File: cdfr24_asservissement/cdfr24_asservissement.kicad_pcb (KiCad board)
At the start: 2 copper layers, 102 x 82.8 mm, 106 parts, among them J1 Connecteur batterie, J10 Conn_01x05, J11 Conn_01x03, J12 Conn_01x05, J13 Conn_01x03, J14 Conn_ST_STDC14, J15 Free Connecteur, J2 Conn_01x03, J3 Connecteur Programmation, J4 Connecteur Odométrie, J5 Free Connecteur, J6 Connecteur Odométrie, J7 Conn_01x03, J8 Conn_01x02, J9 Conn_01x02, Q1 Q_NMOS_GDS, U1 LM317_SOT-223, U2 LMR16020PDDA, U3 STM32F401RCTx, U4 LSM6DSL, Y1 Crystal_GND24

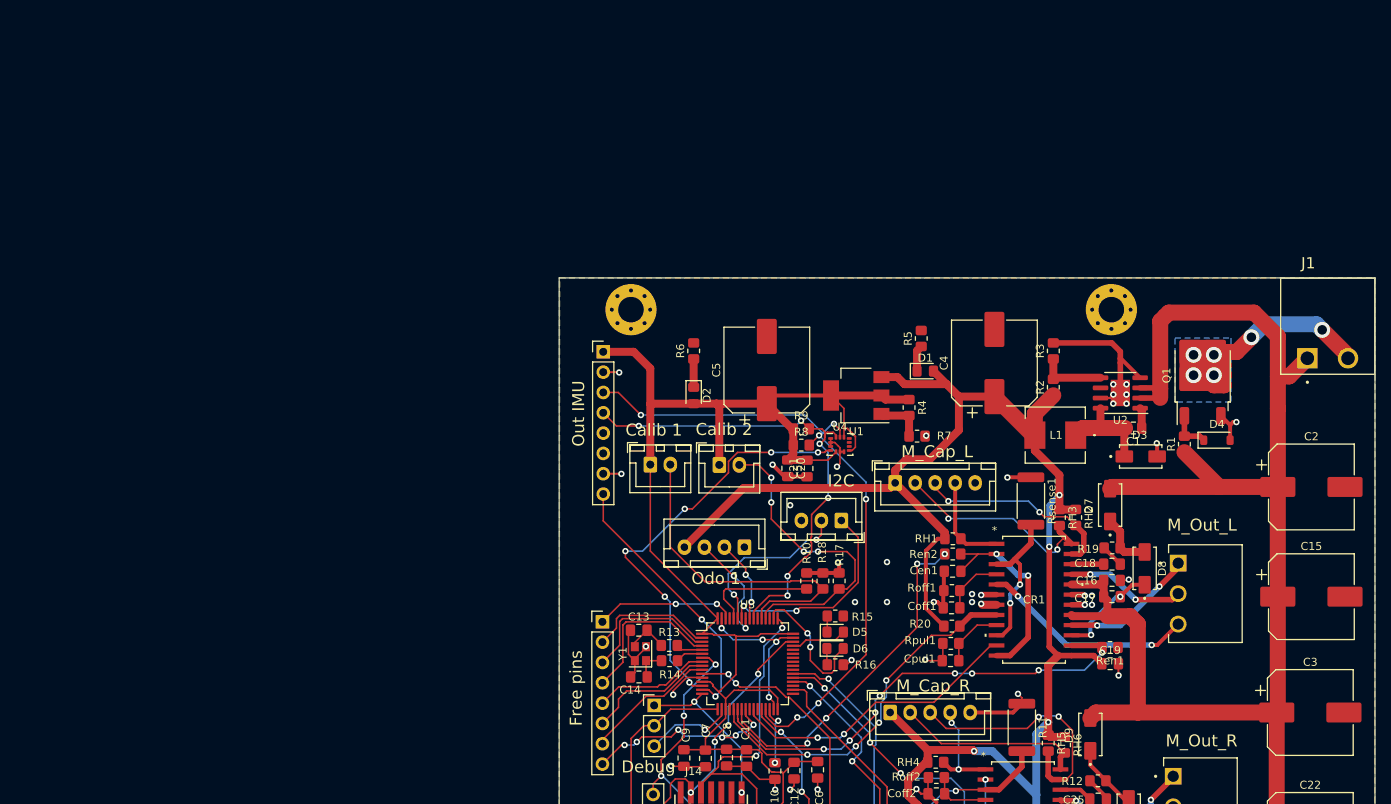
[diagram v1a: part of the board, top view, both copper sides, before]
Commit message: Change 5v to 3.3v regulator to ST product
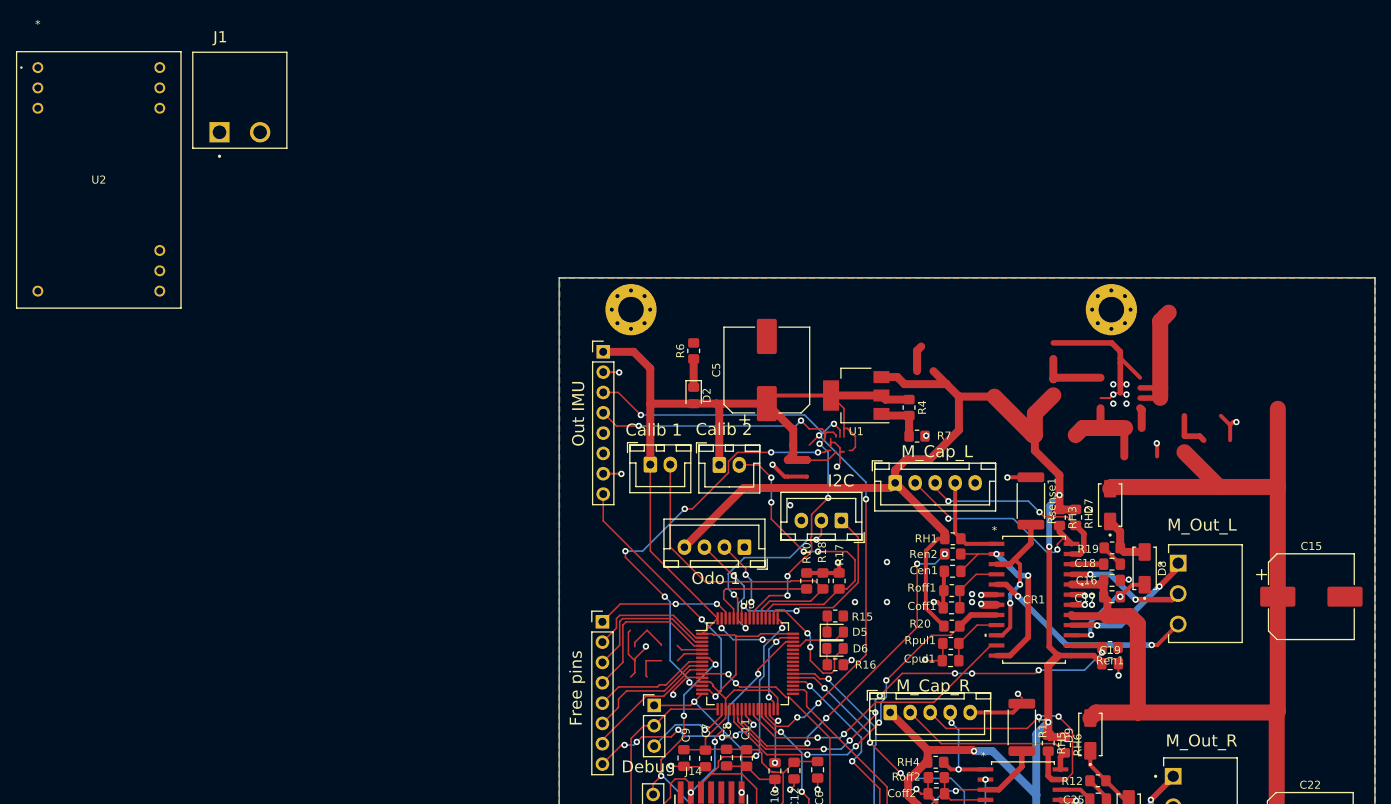
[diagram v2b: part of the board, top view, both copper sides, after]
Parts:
- removed C1, C20, C21: 100nF, Capacitor_SMD:C_0805_2012Metric_Pad1.18x1.45mm_HandSolder
- removed C13, C14: 10pF, Capacitor_SMD:C_0805_2012Metric_Pad1.18x1.45mm_HandSolder
- removed C2, C3: 470uF, Capacitor_SMD:CP_Elec_10x10.5
- removed C4: 220uF, Capacitor_SMD:CP_Elec_10x10.5
- removed D1: LED, LED_SMD:LED_0805_2012Metric_Pad1.15x1.40mm_HandSolder
- removed D3: DIODE, B170B:DIOM505270X240
- removed D4: D_Zener, Diode_SMD:D_SOD-123
- removed L1: 10uH, IHLP2525CZER100M01:IND_IHLP_2525_CZ-M
- removed Q1: Q_NMOS_GDS, Package_TO_SOT_SMD:TO-252-2
- removed R1, R2, R8, R9: 56k, Resistor_SMD:R_0805_2012Metric_Pad1.20x1.40mm_HandSolder
- removed R13, R14, R3: 10k, Resistor_SMD:R_0805_2012Metric_Pad1.20x1.40mm_HandSolder
- removed R5: 220, Resistor_SMD:R_0805_2012Metric_Pad1.20x1.40mm_HandSolder
- removed U4: LSM6DSL, Package_LGA:LGA-14_3x2.5mm_P0.5mm_LayoutBorder3x4y
- removed Y1: Crystal_GND24, Crystal:Crystal_SMD_2520-4Pin_2.5x2.0mm
- U2: value LMR16020PDDA -> TVN 5-2411WI; footprint Package_SO:SOIC-8-1EP_3.9x4.9mm_P1.27mm_EP2.41x3.3mm -> TVN_5WI_SINGLE_TRP:TVN_5WI_SINGLE_TRP
- moved U2 141.3 mm to (2.86, 2.19), turned to 0 degrees
- moved J1 138.9 mm to (25.6, 10.3)
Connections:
- J1 pad 2: /InputVoltage -> GND
- J15 pad 8: /IMU_INT2 -> /IMU_INT1
- U2 pad 1: Net-(U2-BOOT) -> +BATT
- U2 pad 3: +BATT -> unconnected-(U2-CASE-Pad3)
- U3 pad 15: /IMU_INT2 -> unconnected-(U3-PA1-Pad15)
- U3 pad 5: Net-(U3-PH0) -> unconnected-(U3-PH0-Pad5)
- U3 pad 6: Net-(U3-PH1) -> unconnected-(U3-PH1-Pad6)
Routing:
- net (no net): track 0.00 -> 41.5 mm
- net /IMU_INT1: track 53.4 -> 87.1 mm, vias 6 -> 8
- net /IMU_INT2: track 33.7 -> 0.00 mm, vias 2 -> 0
- net /InputVoltage: track 33.6 -> 0.00 mm, vias 6 -> 0
- net +BATT: track 213.9 -> 185.4 mm
- net Net-(D3-A): track 12.6 -> 0.00 mm
- net Net-(U2-FB): track 8.52 -> 0.00 mm
- net Net-(C13-Pad2): track 5.33 -> 0.00 mm
- net Net-(D4-K): track 5.16 -> 0.00 mm
- net Net-(C14-Pad1): track 4.03 -> 0.00 mm
- net unconnected-(U3-PH1-Pad6): track 0.00 -> 3.45 mm
- net Net-(U3-PH1): track 3.45 -> 0.00 mm
- net unconnected-(U3-PH0-Pad5): track 0.00 -> 3.34 mm
- net Net-(U3-PH0): track 3.34 -> 0.00 mm
- net Net-(D1-K): track 3.30 -> 0.00 mm
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- removed copper zone on B.Cu, net /InputVoltage

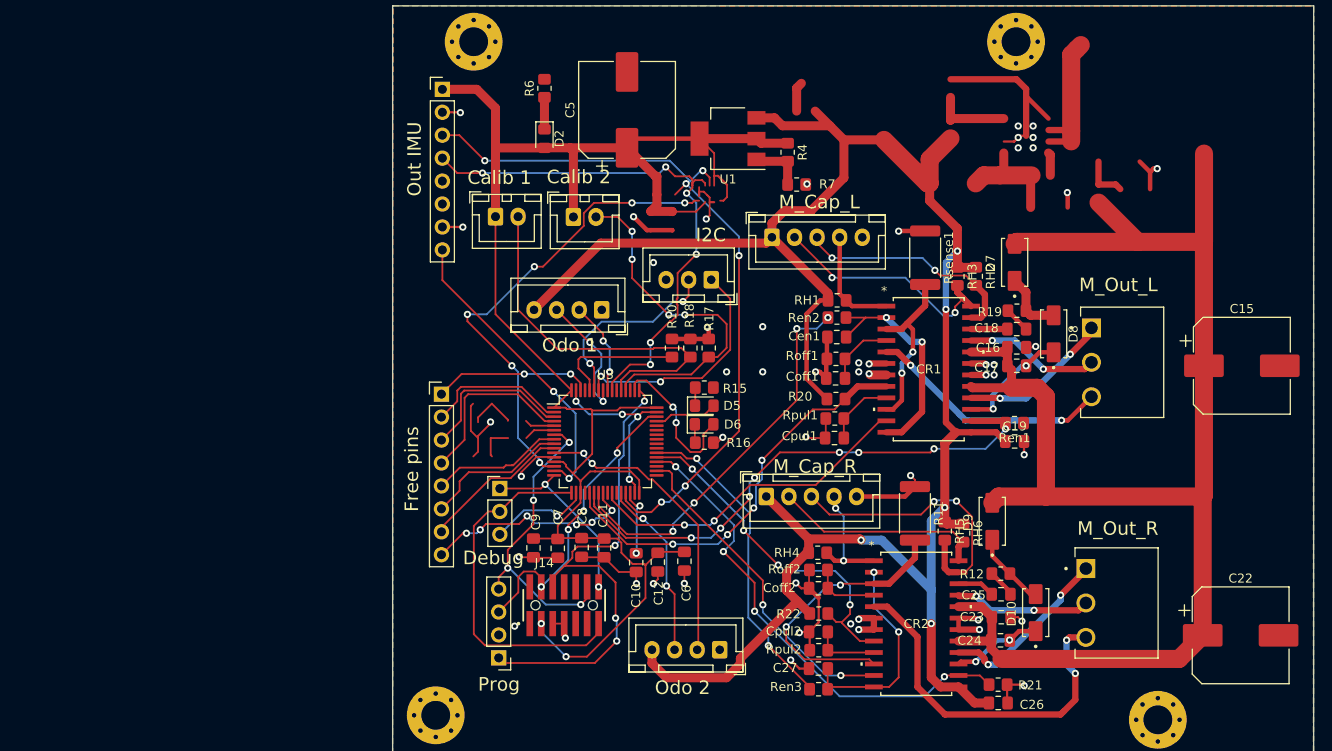
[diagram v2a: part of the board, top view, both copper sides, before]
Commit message: Change STM32 pins
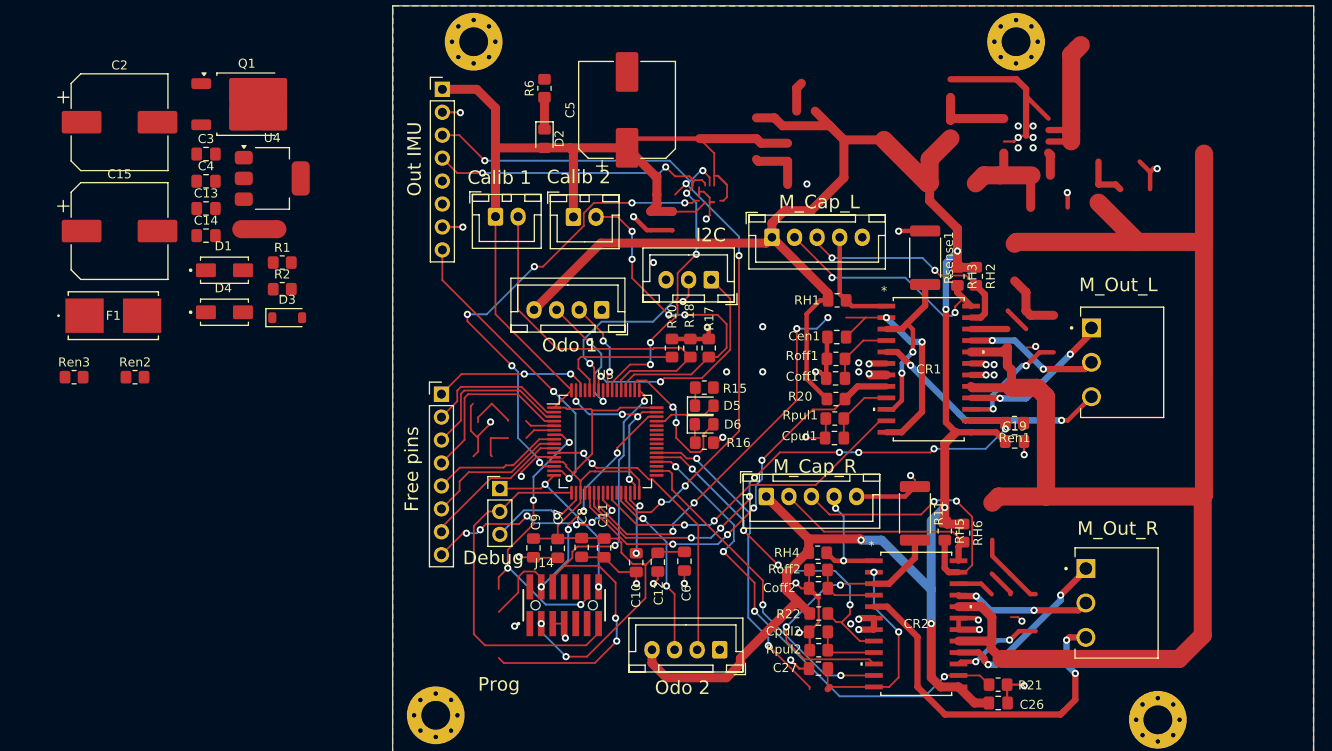
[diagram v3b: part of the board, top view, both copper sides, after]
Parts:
- removed C16, C23: 100n, Capacitor_SMD:C_0805_2012Metric_Pad1.18x1.45mm_HandSolder
- removed C17, C24: 220n, Capacitor_SMD:C_0805_2012Metric_Pad1.18x1.45mm_HandSolder
- removed C18, C25: 10n, Capacitor_SMD:C_0805_2012Metric_Pad1.18x1.45mm_HandSolder
- removed C22: 100u, Capacitor_SMD:CP_Elec_10x10.5
- removed D10, D7, D8, D9: DIODE, B170B:DIOM505270X240
- removed J3: Connecteur Programmation, Connector_PinHeader_2.54mm:PinHeader_1x04_P2.54mm_Vertical
- removed R12, R19: 100, Resistor_SMD:R_0805_2012Metric_Pad1.20x1.40mm_HandSolder
- removed R4: 2k4, Resistor_SMD:R_0805_2012Metric_Pad1.20x1.40mm_HandSolder
- removed R7: 3k9, Resistor_SMD:R_0805_2012Metric_Pad1.20x1.40mm_HandSolder
- removed U1: LM317_SOT-223, Package_TO_SOT_SMD:SOT-223-3_TabPin2
- added C13: 10n, Capacitor_SMD:C_0805_2012Metric_Pad1.18x1.45mm_HandSolder, F.Cu at (47.4, 50.9)
- added C14: 100n, Capacitor_SMD:C_0805_2012Metric_Pad1.18x1.45mm_HandSolder, F.Cu at (47.4, 53.9)
- added C2: 220u, Capacitor_SMD:CP_Elec_10x10.5, F.Cu at (37.8, 41.4)
- added C3: 100n, Capacitor_SMD:C_0805_2012Metric_Pad1.18x1.45mm_HandSolder, F.Cu at (47.4, 44.9)
- added C4: 100n, Capacitor_SMD:C_0805_2012Metric_Pad1.18x1.45mm_HandSolder, F.Cu at (47.4, 47.9)
- added D1: DIODE, B170B:DIOM505270X240, F.Cu at (49.4, 57.8)
- added D3: D_Zener, Diode_SMD:D_SOD-123, F.Cu at (56.4, 63.0)
- added D4: DIODE, B170B:DIOM505270X240, F.Cu at (49.4, 62.4)
- added F1: 01550900M, LittleFuse:FUSE_01550900M_LTF, F.Cu at (37.1, 62.8)
- added NT1: NetTie_2, NetTie:NetTie-2_SMD_Pad2.0mm, F.Cu at (53.3, 53.2)
- added Q1: Q_NMOS_GDS, Package_TO_SOT_SMD:TO-252-2, F.Cu at (51.9, 39.4)
- added R1: 56k, Resistor_SMD:R_0805_2012Metric_Pad1.20x1.40mm_HandSolder, F.Cu at (55.8, 56.9)
- added R2: 100, Resistor_SMD:R_0805_2012Metric_Pad1.20x1.40mm_HandSolder, F.Cu at (55.8, 59.9)
- added U4: LD1117S33TR_SOT223, Package_TO_SOT_SMD:SOT-223-3_TabPin2, F.Cu at (54.7, 47.6)
- C5: value 100uF -> 10uF
- R11, Rsense1: value 0.3 -> 0.15
- Ren2, Ren3: value 100k -> 10k
- moved C15 125.2 mm to (37.8, 53.4)
- moved Ren3 89.4 mm to (32.8, 69.6)
- moved Ren2 78.0 mm to (39.5, 69.6)
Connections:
- C15 pad 1: +BATT -> +5V
- C19 pad 1: +5V -> /Vref_DAC
- C26 pad 1: +5V -> /Vref_DAC
- CR1 pad 13: +5V -> /Vref_DAC
- CR1 pad 15: /left_driver/Vboot -> /Vboot
- CR1 pad 17: +BATT -> /Vsab
- CR1 pad 20: +BATT -> /Vsab
- CR1 pad 22: /left_driver/Vcp -> /Vcp_L
- CR2 pad 13: +5V -> /Vref_DAC
- CR2 pad 15: /right_driver/Vboot -> /Vboot
- CR2 pad 17: +BATT -> /Vsab
- CR2 pad 20: +BATT -> /Vsab
- J1 pad 2: GND -> Net-(J1-Pin_2)
- J14 pad 8: unconnected-(J14-JTDO/SWO-Pad8) -> SWO
- J15 pad 7: GND -> /INT_MAG
- J15 pad 8: /IMU_INT1 -> /INT_IMU
- J4 pad 2: odometrie2 -> Net-(J4-Pin_2)
- R11 pad 1: GND -> GNDPWR
- R20 pad 2: +5V -> +3.3V
- R22 pad 2: +5V -> +3.3V
- Rsense1 pad 1: GND -> GNDPWR
- U2 pad 23: GND -> GNDPWR
- U2 pad 24: GND -> GNDPWR
- U3 pad 10: Free7 -> unconnected-(U3-PC2-Pad10)
- U3 pad 11: odometrie2 -> /INT_IMU
- U3 pad 14: /IMU_INT1 -> Net-(J4-Pin_2)
- U3 pad 15: unconnected-(U3-PA1-Pad15) -> Net-(J4-Pin_3)
- U3 pad 21: /TACHO_L -> unconnected-(U3-PA5-Pad21)
- U3 pad 22: /BRAKE_L -> unconnected-(U3-PA6-Pad22)
- U3 pad 23: /EN_L -> unconnected-(U3-PA7-Pad23)
- U3 pad 24: Free8 -> /INT_MAG
- U3 pad 26: /FWD_L -> unconnected-(U3-PB0-Pad26)
- U3 pad 27: unconnected-(U3-PB1-Pad27) -> /EN_R
- U3 pad 28: Net-(J4-Pin_3) -> /BRAKE_R
- U3 pad 29: /IMU_SCL -> /TACHO_R
- U3 pad 34: /FWD_R -> unconnected-(U3-PB13-Pad34)
- U3 pad 35: unconnected-(U3-PB14-Pad35) -> /EN_L
- U3 pad 36: /BRAKE_R -> /BRAKE_L
- U3 pad 37: /TACHO_R -> /TACHO_L
- U3 pad 38: /EN_R -> unconnected-(U3-PC7-Pad38)
- U3 pad 40: unconnected-(U3-PC9-Pad40) -> /IMU_SDA
- U3 pad 41: unconnected-(U3-PA8-Pad41) -> /IMU_SCL
- U3 pad 42: unconnected-(U3-PA9-Pad42) -> /FWD_L
- U3 pad 43: unconnected-(U3-PA10-Pad43) -> /FWD_R
- U3 pad 44: unconnected-(U3-PA11-Pad44) -> /Vref_DAC
- U3 pad 55: /IMU_SDA -> SWO
- U3 pad 56: Net-(J6-Pin_2) -> unconnected-(U3-PB4-Pad56)
- U3 pad 57: Net-(J6-Pin_3) -> unconnected-(U3-PB5-Pad57)
- U3 pad 58: /I2C_CLK -> Net-(J6-Pin_2)
- U3 pad 59: /I2C_SDA -> Net-(J6-Pin_3)
- U3 pad 61: unconnected-(U3-PB8-Pad61) -> /I2C_CLK
- U3 pad 62: Free1 -> /I2C_SDA
- U3 pad 8: Free5 -> unconnected-(U3-PC0-Pad8)
- U3 pad 9: Free6 -> unconnected-(U3-PC1-Pad9)
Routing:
- net /Vsab: track 0.00 -> 169.2 mm
- net +BATT: track 185.4 -> 16.2 mm
- net /IMU_INT1: track 87.1 -> 0.00 mm, vias 8 -> 0
- net (no net): track 41.5 -> 102.3 mm, vias 0 -> 2
- net Net-(J4-Pin_2): track 0.00 -> 53.4 mm, vias 0 -> 6
- net unconnected-(U3-PA7-Pad23): track 0.00 -> 43.2 mm, vias 0 -> 4
- net /EN_L: track 43.2 -> 0.00 mm, vias 4 -> 0
- net unconnected-(U3-PC7-Pad38): track 0.00 -> 35.6 mm, vias 0 -> 2
- net /EN_R: track 35.6 -> 0.00 mm, vias 2 -> 0
- net Net-(J4-Pin_3): track 20.1 -> 53.8 mm, vias 2 -> 4
- net odometrie2: track 33.2 -> 0.00 mm, vias 2 -> 0
- net /Vboot: track 0.00 -> 22.8 mm, vias 0 -> 4
- net /left_driver/Vboot: track 12.8 -> 0.00 mm, vias 2 -> 0
- net /right_driver/Vboot: track 10.0 -> 0.00 mm, vias 2 -> 0
- net Net-(D10-K): track 8.34 -> 0.00 mm
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
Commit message: Place components
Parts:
- removed C26: 100n, Capacitor_SMD:C_0805_2012Metric_Pad1.18x1.45mm_HandSolder
- removed C27: 5.6n, Capacitor_SMD:C_0805_2012Metric_Pad1.18x1.45mm_HandSolder
- removed R17, R18, R20, R21, R22: 10k, Resistor_SMD:R_0805_2012Metric_Pad1.20x1.40mm_HandSolder
- removed U4: LD1117S33TR_SOT223, Package_TO_SOT_SMD:SOT-223-3_TabPin2
- added C1: 100nF, Capacitor_SMD:C_0805_2012Metric_Pad1.18x1.45mm_HandSolder, F.Cu at (195.8, 140.0)
- added C16: ..., Capacitor_SMD:C_0805_2012Metric_Pad1.18x1.45mm_HandSolder, F.Cu at (204.3, 90.4)
- added C17: 4.7uF, Capacitor_SMD:C_0805_2012Metric_Pad1.18x1.45mm_HandSolder, F.Cu at (194.4, 111.6)
- added C18: 100n, Capacitor_SMD:C_0805_2012Metric_Pad1.18x1.45mm_HandSolder, F.Cu at (242.1, 86.9)
- added Cen2: 5.6n, Capacitor_SMD:C_0805_2012Metric_Pad1.18x1.45mm_HandSolder, F.Cu at (224.5, 117.9)
- added D7: LED, LED_SMD:LED_0805_2012Metric_Pad1.15x1.40mm_HandSolder, F.Cu at (201.2, 81.3)
- added J3: Conn_01x03, TerminalBlockBend:CUI_TBP02R1-381-03BE, F.Cu at (252.6, 78.0)
- added R12: 10k, Resistor_SMD:R_0805_2012Metric_Pad1.20x1.40mm_HandSolder, F.Cu at (199.9, 91.8)
- added R13: 10k, Resistor_SMD:R_0805_2012Metric_Pad1.20x1.40mm_HandSolder, F.Cu at (217.9, 85.4)
- added R14: 0.15, Resistor_SMD:R_2512_6332Metric, F.Cu at (231.1, 98.4)
- added R3: 150, Resistor_SMD:R_0805_2012Metric_Pad1.20x1.40mm_HandSolder, F.Cu at (200.7, 131.5)
- added R4: 100, Resistor_SMD:R_0805_2012Metric_Pad1.20x1.40mm_HandSolder, F.Cu at (246.4, 83.2)
- added R5: 10k, Resistor_SMD:R_0805_2012Metric_Pad1.20x1.40mm_HandSolder, F.Cu at (189.5, 92.0)
- added R7: ..., Resistor_SMD:R_0805_2012Metric_Pad1.20x1.40mm_HandSolder, F.Cu at (204.3, 94.2)
- added R8: 220, Resistor_SMD:R_0805_2012Metric_Pad1.20x1.40mm_HandSolder, F.Cu at (198.1, 77.2)
- added R9: 220, Resistor_SMD:R_0805_2012Metric_Pad1.20x1.40mm_HandSolder, F.Cu at (201.2, 77.2)
- added SW1: SW_DIP_x02, Button_Switch_SMD:SW_DIP_SPSTx02_Slide_Copal_CHS-02B_W7.62mm_P1.27mm, F.Cu at (167.8, 121.7)
- added U1: LD1117S33TR_SOT223, Package_TO_SOT_SMD:SOT-223-3_TabPin2, F.Cu at (194.6, 134.0)
- C10: value 4.7uF -> 100nF
- C11: value 10nF -> 100nF
- C12: value 1uF -> 100nF
- C13: value 10n -> 10uF
- C14: value 100n -> 10nF
- C15: value 100u -> 1uF; footprint Capacitor_SMD:CP_Elec_10x10.5 -> Capacitor_SMD:C_0805_2012Metric_Pad1.18x1.45mm_HandSolder
- C2: value 220u -> 10uF; footprint Capacitor_SMD:CP_Elec_10x10.5 -> Capacitor_SMD:C_0805_2012Metric_Pad1.18x1.45mm_HandSolder
- C3: value 100n -> 220u; footprint Capacitor_SMD:C_0805_2012Metric_Pad1.18x1.45mm_HandSolder -> Capacitor_SMD:CP_Elec_10x10.5
- C5: value 10uF -> 100n; footprint Capacitor_SMD:CP_Elec_10x10.5 -> Capacitor_SMD:C_0805_2012Metric_Pad1.18x1.45mm_HandSolder
- C6: value 100nF -> 100n
- C7: value 100nF -> 10n
- D1: value DIODE -> LED; footprint B170B:DIOM505270X240 -> LED_SMD:LED_0805_2012Metric_Pad1.15x1.40mm_HandSolder
- D3: value D_Zener -> D_Filled; footprint Diode_SMD:D_SOD-123 -> B170B:DIOM505270X240
- D4: value DIODE -> D_Zener; footprint B170B:DIOM505270X240 -> Diode_SMD:D_SOD-123
- D5: value LED -> D_Filled; footprint LED_SMD:LED_0805_2012Metric_Pad1.15x1.40mm_HandSolder -> B170B:DIOM505270X240
- J10, J12: value Conn_01x05 -> Connecteur Odométrie; footprint Connector_JST:JST_XH_B5B-XH-A_1x05_P2.50mm_Vertical -> Connector_JST:JST_XH_B4B-XH-A_1x04_P2.50mm_Vertical
- J11: footprint TerminalBlockBend:CUI_TBP02R1-381-03BE -> Connector_PinHeader_2.54mm:PinHeader_1x03_P2.54mm_Vertical
- J13: footprint TerminalBlockBend:CUI_TBP02R1-381-03BE -> Connector_JST:JST_XH_B3B-XH-A_1x03_P2.50mm_Vertical
- J14: value Conn_ST_STDC14 -> Conn_01x02; footprint FTSH-107-01-L-DV-K-A:SAMTEC_FTSH-107-01-L-DV-K-A -> Connector_JST:JST_XH_B2B-XH-A_1x02_P2.50mm_Vertical
- J15: value Free Connecteur -> Conn_01x02; footprint Connector_PinHeader_2.54mm:PinHeader_1x08_P2.54mm_Vertical -> Connector_JST:JST_XH_B2B-XH-A_1x02_P2.50mm_Vertical
- J2: value Conn_01x03 -> Conn_01x05; footprint Connector_PinHeader_2.54mm:PinHeader_1x03_P2.54mm_Vertical -> Connector_JST:JST_XH_B5B-XH-A_1x05_P2.50mm_Vertical
- J4: value Connecteur Odométrie -> Conn_01x08_Pin; footprint Connector_JST:JST_XH_B4B-XH-A_1x04_P2.50mm_Vertical -> Connector_PinHeader_2.54mm:PinHeader_1x08_P2.54mm_Vertical
- J5: value Free Connecteur -> Conn_ST_STDC14; footprint Connector_PinHeader_2.54mm:PinHeader_1x08_P2.54mm_Vertical -> FTSH-107-01-L-DV-K-A:SAMTEC_FTSH-107-01-L-DV-K-A
- J6: value Connecteur Odométrie -> Conn_01x05; footprint Connector_JST:JST_XH_B4B-XH-A_1x04_P2.50mm_Vertical -> Connector_JST:JST_XH_B5B-XH-A_1x05_P2.50mm_Vertical
- J7: value Conn_01x03 -> Connecteur Programmation; footprint Connector_JST:JST_XH_B3B-XH-A_1x03_P2.50mm_Vertical -> Connector_PinHeader_2.54mm:PinHeader_1x04_P2.54mm_Vertical
- J8: value Conn_01x02 -> Conn_01x03; footprint Connector_JST:JST_XH_B2B-XH-A_1x02_P2.50mm_Vertical -> TerminalBlockBend:CUI_TBP02R1-381-03BE
- J9: value Conn_01x02 -> Conn_01x08_Pin; footprint Connector_JST:JST_XH_B2B-XH-A_1x02_P2.50mm_Vertical -> Connector_PinHeader_2.54mm:PinHeader_1x08_P2.54mm_Vertical
- R10: value 10k -> 2.2k
- R11: value 0.15 -> 10k; footprint Resistor_SMD:R_2512_6332Metric -> Resistor_SMD:R_0805_2012Metric_Pad1.20x1.40mm_HandSolder
- R15, R16: value 220 -> 10k
- R2: value 100 -> 150
- R6: value 150 -> 2.2k
- Ren2, Ren3: value 10k -> 100k
- moved U2 263.5 mm to (234.9, 127.0), turned to -90 degrees
- moved J1 252.8 mm to (250.5, 125.7), turned to -90 degrees
- moved Q1 216.6 mm to (243.8, 139.7), turned to -90 degrees
- moved F1 214.7 mm to (243.8, 120.7), turned to 90 degrees
- moved C3 209.0 mm to (249.5, 97.8), turned to 180 degrees
- moved C4 206.6 mm to (246.0, 104.8), turned to 180 degrees
- moved D4 206.1 mm to (243.8, 130.8), turned to 180 degrees
- moved R1 201.1 mm to (243.9, 128.3)
- moved D3 200.6 mm to (255.0, 90.4), turned to 180 degrees
- moved NT1 196.9 mm to (245.5, 95.7), turned to 90 degrees
- moved Ren3 192.1 mm to (222.2, 101.3)
- moved Ren2 182.9 mm to (222.2, 77.3)
- moved C2 177.9 mm to (188.0, 136.8), turned to 90 degrees
- moved J8 174.3 mm to (252.6, 109.2), turned to -90 degrees
- moved C5 162.5 mm to (239.5, 112.2), turned to -90 degrees
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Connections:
- C10 pad 1: Net-(U3-VCAP1) -> +3.3V
- C13 pad 1: Net-(C13-Pad1) -> +3.3V
- C13 pad 2: /Vcp_L -> GND
- C14 pad 1: /Vsab -> +3.3V
- C14 pad 2: /Vboot -> GND
- C15 pad 1: +5V -> +3.3V
- C2 pad 1: /Vsab -> +3.3V
- C2 pad 2: GNDPWR -> GND
- C4 pad 2: /Vboot -> GNDPWR
- C5 pad 1: +3.3V -> /Vsab
- C5 pad 2: GND -> /Vboot
- C6 pad 1: +3.3V -> /Vsab
- C6 pad 2: GND -> /Vboot
- C7 pad 1: +3.3V -> Net-(C7-Pad1)
- C7 pad 2: GND -> /Vcp_L
- D1 pad 1: /Vsab -> Net-(D1-K)
- D1 pad 2: Net-(D1-A) -> +3.3V
- D2 pad 2: +3.3V -> +5V
- D3 pad 2: GNDPWR -> /Vsab
- D4 pad 1: Net-(D1-A) -> Net-(D4-K)
- D4 pad 2: /Vboot -> GNDPWR
- D5 pad 1: Net-(D5-K) -> /Vboot
- D5 pad 2: Net-(D5-A) -> Net-(D3-K)
- J10 pad 1: +5V -> GND
- J10 pad 2: /left_driver/H3 -> Net-(J10-Pin_2)
- J10 pad 3: /left_driver/H2 -> Net-(J10-Pin_3)
- J10 pad 4: /left_driver/H1 -> +5V
- J11 pad 1: /left_driver/OUT3 -> /TX
- J11 pad 2: /left_driver/OUT2 -> /RX
- J11 pad 3: /left_driver/OUT1 -> GND
- J12 pad 1: +5V -> GND
- J12 pad 2: /right_driver/H3 -> Net-(J12-Pin_2)
- J12 pad 3: /right_driver/H2 -> Net-(J12-Pin_3)
- J12 pad 4: /right_driver/H1 -> +5V
- J13 pad 1: /right_driver/OUT3 -> /I2C_CLK
- J13 pad 2: /right_driver/OUT2 -> /I2C_SDA
- J13 pad 3: /right_driver/OUT1 -> GND
- J14 pad 1: unconnected-(J14-NC-Pad1) -> +3.3V
- J14 pad 2: unconnected-(J14-NC-Pad2) -> Net-(J14-Pin_2)
- J15 pad 2: GND -> Net-(J15-Pin_2)
- J2 pad 1: /TX -> +5V
- J2 pad 2: /RX -> /left_driver/H3
- J2 pad 3: GND -> /left_driver/H2
- J4 pad 1: GND -> +3.3V
- J4 pad 2: Net-(J4-Pin_2) -> GND
- J4 pad 3: Net-(J4-Pin_3) -> /IMU_SCL
- J4 pad 4: +5V -> /IMU_SDA
- J5 pad 1: Free1 -> unconnected-(J5-NC-Pad1)
- J5 pad 2: Free2 -> unconnected-(J5-NC-Pad2)
- J5 pad 3: Free3 -> +3.3V
- J5 pad 4: Free4 -> SWDIO
- J5 pad 5: Free5 -> GND
- J5 pad 6: Free6 -> SWCLK
- J5 pad 7: Free7 -> GND
- J5 pad 8: Free8 -> SWO
- J6 pad 1: GND -> +5V
- J6 pad 2: Net-(J6-Pin_2) -> /right_driver/H3
- J6 pad 3: Net-(J6-Pin_3) -> /right_driver/H2
- J6 pad 4: +5V -> /right_driver/H1
- J7 pad 1: /I2C_CLK -> GND
- J7 pad 2: /I2C_SDA -> SWCLK
- J7 pad 3: GND -> SWDIO
- J8 pad 1: +3.3V -> /right_driver/OUT3
- J8 pad 2: Net-(J8-Pin_2) -> /right_driver/OUT2
- J9 pad 1: +3.3V -> unconnected-(J9-Pin_1-Pad1)
- J9 pad 2: Net-(J9-Pin_2) -> Free2
- Q1 pad 1: Net-(D3-K) -> Net-(D4-K)
- R1 pad 2: Net-(D3-K) -> Net-(D4-K)
- R10 pad 1: GND -> /IMU_SDA
- R10 pad 2: Net-(U3-BOOT0) -> +3.3V
- R11 pad 1: GNDPWR -> GND
- R11 pad 2: Net-(CR2B-SENSEA) -> Net-(J14-Pin_2)
- R15 pad 1: Net-(D5-K) -> GND
- R15 pad 2: GND -> /BRAKE_R
- R16 pad 1: Net-(D6-K) -> /TACHO_R
- R16 pad 2: GND -> +3.3V
- R2 pad 1: Net-(D1-A) -> Net-(D1-K)
- R2 pad 2: Net-(C13-Pad1) -> GND
- R6 pad 1: Net-(D2-K) -> /IMU_SCL
- R6 pad 2: GND -> +3.3V
- U3 pad 14: Net-(J4-Pin_2) -> Net-(J10-Pin_2)
- U3 pad 15: Net-(J4-Pin_3) -> Net-(J10-Pin_3)
- U3 pad 44: /Vref_DAC -> Net-(U3-PA11)
- U3 pad 45: Net-(D5-A) -> Net-(D6-A)
- U3 pad 50: Net-(D6-A) -> Net-(D7-A)
- U3 pad 52: Net-(J8-Pin_2) -> Net-(J14-Pin_2)
- U3 pad 53: Net-(J9-Pin_2) -> Net-(J15-Pin_2)
- U3 pad 58: Net-(J6-Pin_2) -> Net-(J12-Pin_2)
- U3 pad 59: Net-(J6-Pin_3) -> Net-(J12-Pin_3)
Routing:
- net +5V: track 233.1 -> 0.00 mm, vias 5 -> 0
- net +3.3V: track 189.4 -> 0.00 mm, vias 2 -> 0
- net /Vsab: track 169.2 -> 0.00 mm
- net GND: track 168.7 -> 0.00 mm, vias 54 -> 0
- net (no net): track 102.3 -> 0.00 mm, vias 2 -> 0
- net /IMU_SCL: track 83.3 -> 0.00 mm, vias 6 -> 0
- net /IMU_SDA: track 60.9 -> 0.00 mm, vias 6 -> 0
- net /BRAKE_L: track 58.5 -> 0.00 mm, vias 8 -> 0
- net SWCLK: track 55.8 -> 0.00 mm, vias 4 -> 0
- net /BRAKE_R: track 54.2 -> 0.00 mm, vias 4 -> 0
- net Net-(J4-Pin_3): track 53.8 -> 0.00 mm, vias 4 -> 0
- net Net-(J4-Pin_2): track 53.4 -> 0.00 mm, vias 6 -> 0
- net /TACHO_L: track 45.9 -> 0.00 mm, vias 4 -> 0
- net unconnected-(U3-PA7-Pad23): track 43.2 -> 0.00 mm, vias 4 -> 0
- net Net-(J9-Pin_2): track 41.5 -> 0.00 mm
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- removed copper zone on B.Cu, net GND
- removed copper zone on F.Cu, net GND
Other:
- board size 102 x 82.8 mm -> 101.6 x 78.6 mm
- board text removed: "Calib 1"
- board text removed: "Calib 2"
- board text removed: "Debug"
- board text removed: "Free pins"
- board text removed: "I2C"
- board text removed: "M_Cap_L"
- board text removed: "M_Cap_R"
- board text removed: "M_Out_L"
- board text removed: "M_Out_R"
- board text removed: "Odo 1"
- board text removed: "Odo 2"
- board text removed: "Out IMU"
- board text removed: "Prog"
